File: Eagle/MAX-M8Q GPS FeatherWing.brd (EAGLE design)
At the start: 50.8 x 22.9 mm, 28 parts, among them Q1 DMG3415U-7, Q2 2N2222, SW1 KMR2, U1 MAX-M8, X1 uFL

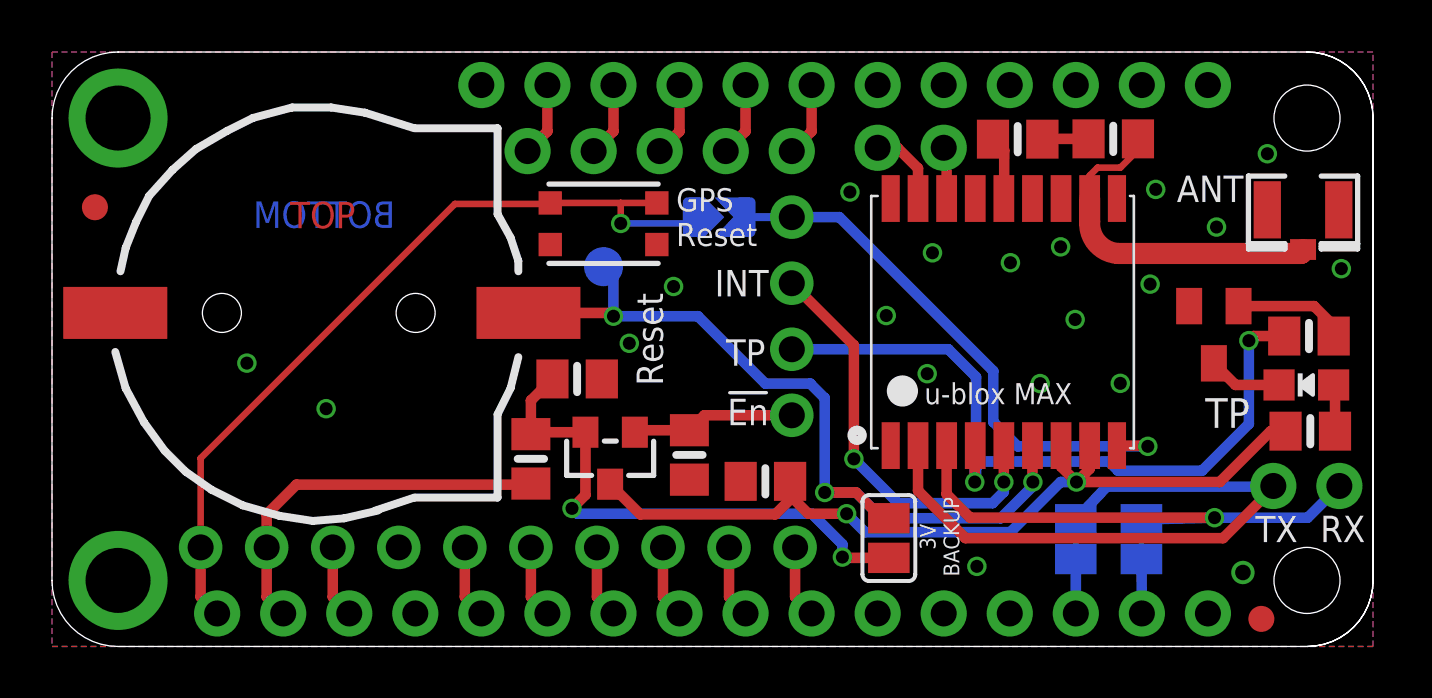
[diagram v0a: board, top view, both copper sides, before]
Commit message: Updated PCB
Updated PCB now includes: pull-up resistors for SCL and SDA; a
decoupling capacitor for VCC_RF; a test pad for SAFEBOOT.
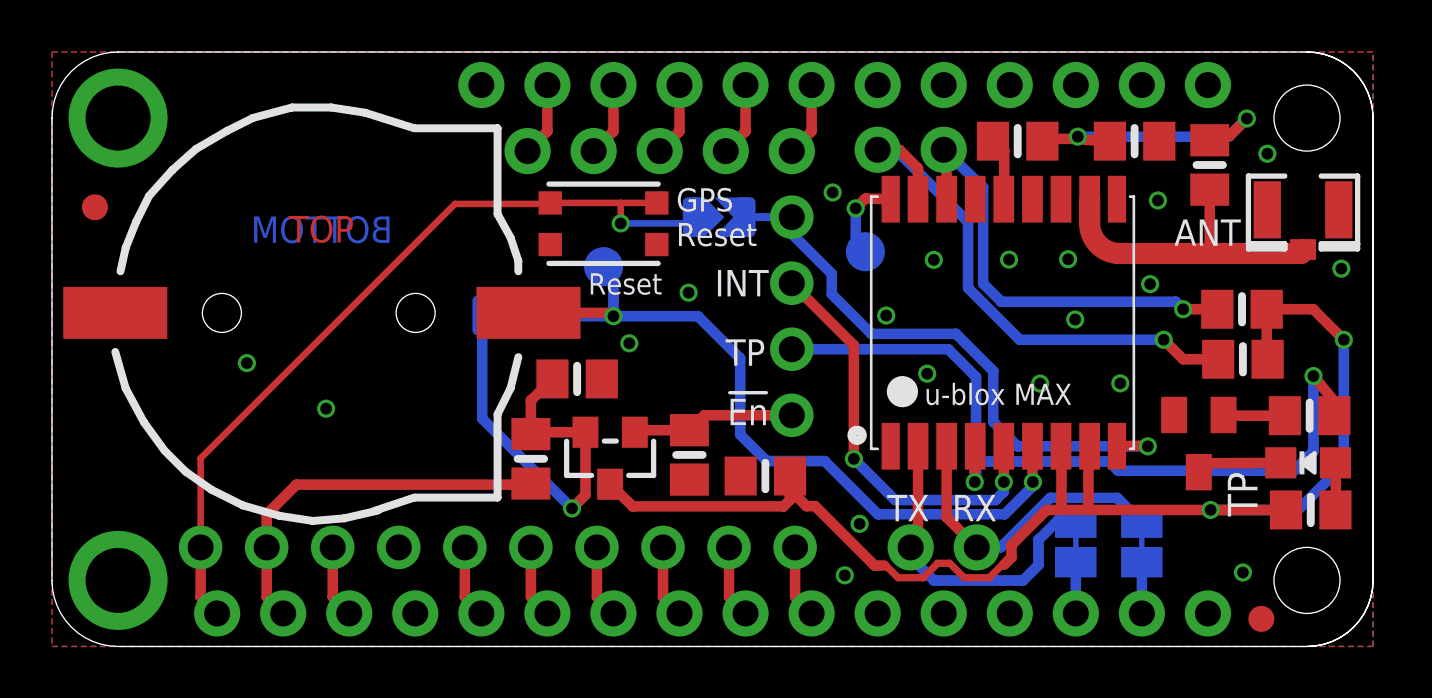
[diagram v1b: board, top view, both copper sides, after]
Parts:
- added C3: 10nF, microbuilder:0805-NO
- added R5, R6: 1K, microbuilder:0805-NO
- added TP2: (no value), microbuilder:TESTPOINT_ROUND_1.5MM
- SJ4: device jumper:SJ -> microbuilder:SOLDERJUMPER_ARROW_NOPASTE
- moved SJ4 16.9 mm to (17.6, 12.7), flipped to the bottom, turned to 0 degrees
- moved JP3 14.1 mm to (34.3, 3.81)
- moved Q2 4.23 mm to (44.1, 7.80)
- moved L1 3.84 mm to (44.5, 18.5), turned to 270 degrees
- moved R3 3.06 mm to (48.4, 8.88), turned to 180 degrees
- moved R1 3.03 mm to (48.4, 5.25)
- moved LED1 3.00 mm to (48.3, 7.06)
- moved C1 0.20 mm to (27.4, 6.55)
- moved SJ3 0.12 mm to (41.9, 4.00)
- moved SJ2 0.12 mm to (39.4, 4.00)
- moved JP5 0.08 mm to (33.0, 19.1)
- moved R4 0.08 mm to (37.1, 19.4)
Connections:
- new net SAFEBOOT: TP2.P$1, U1.18_SAFEBOOT_N
- net GND: now also C3.2
- net GPSVCC: now also R5.2, R6.2
- net N$4: now also C3.1
- net SCL: now also R6.1
- net SDA: now also R5.1
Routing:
- net GPSVCC: track 33.4 -> 53.0 mm
- net SCL: track 3.04 -> 20.9 mm, vias 0 -> 1
- net SDA: track 1.99 -> 17.2 mm, vias 0 -> 1
- net TX: track 25.2 -> 12.7 mm
- net N$4: track 1.78 -> 11.3 mm, vias 0 -> 2
- net RX: track 20.7 -> 11.9 mm, vias 1 -> 0
- net 3.3V: track 21.0 -> 16.6 mm, vias 2 -> 1
- net SAFEBOOT: track 0.00 -> 3.38 mm, vias 0 -> 1
- net TP: track 29.8 -> 31.9 mm
- net N$19: track 4.37 -> 2.37 mm
- net ANT: track 13.3 -> 12.2 mm
- net GRESET: track 21.5 -> 22.3 mm
- net VBACKUP: track 31.8 -> 31.4 mm, vias 3 -> 2
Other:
- board text added: "SAFE BOOT"
